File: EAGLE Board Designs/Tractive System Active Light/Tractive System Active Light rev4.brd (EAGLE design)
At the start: 67.5 x 26.9 mm, 10 parts, among them J1 CONNECTOR-4_μF_S_RA_

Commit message: updated led silkscreen
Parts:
- renumbered U$1 to D1, U$2 to D2, U$3 to D3, U$4 to D4
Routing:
- net N$9: track 16.0 -> 16.6 mm
- net N$7: track 19.6 -> 20.2 mm
- net N$2: track 20.5 -> 20.0 mm

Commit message: Update Tractive System Active Light rev4.brd
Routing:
- net N$2: track 20.0 -> 20.6 mm
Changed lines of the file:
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@@
 <contactref element="D4" pad="B+"/>
 <via x="-19.05" y="16.51" extent="1-16" drill="0.381"/>
-<wire x1="-13.3625" y1="18.685" x2="-13.39710625" y2="18.685" width="0.4064" layer="16"/>
-<wire x1="-13.39710625" y1="18.685" x2="-14.07770625" y2="19.3656" width="0.4064" layer="16"/>
-<wire x1="-14.07770625" y1="19.3656" x2="-16.1944" y2="19.3656" width="0.4064" layer="16"/>
-<wire x1="-16.1944" y1="19.3656" x2="-19.05" y2="16.51" width="0.4064" layer="16"/>
 <wire x1="-19.05" y1="16.51" x2="-20.6175" y2="16.51" width="0.4064" layer="1"/>
 <wire x1="-20.6175" y1="16.51" x2="-28.6025" y2="8.525" width="0.4064" layer="1"/>
+<wire x1="-13.3625" y1="18.685" x2="-13.3625" y2="18.9505" width="0.4064" layer="16"/>
+<wire x1="-13.3625" y1="18.9505" x2="-14.351" y2="19.939" width="0.4064" layer="16"/>
+<wire x1="-14.351" y1="19.939" x2="-15.621" y2="19.939" width="0.4064" layer="16"/>
+<wire x1="-15.621" y1="19.939" x2="-19.05" y2="16.51" width="0.4064" layer="16"/>
 </signal>
 </signals>

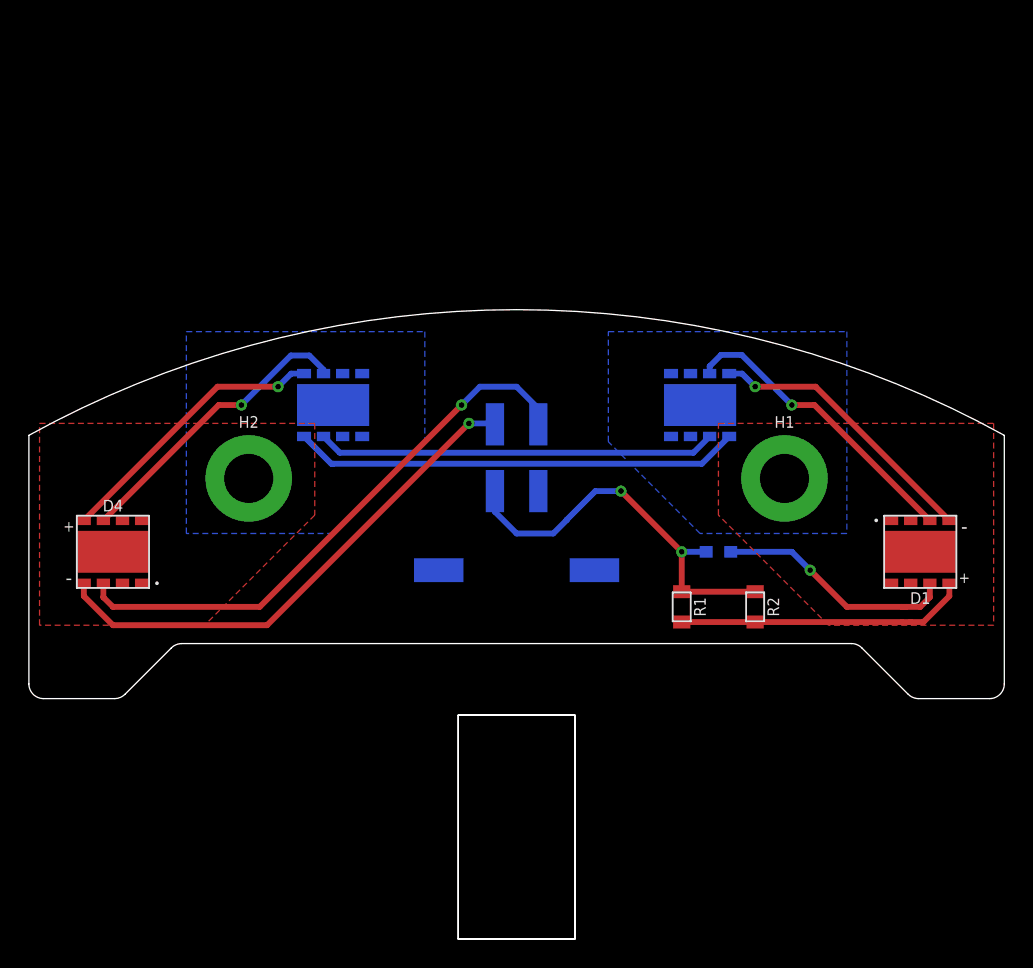
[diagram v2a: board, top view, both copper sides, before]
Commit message: moved connector to face upwards
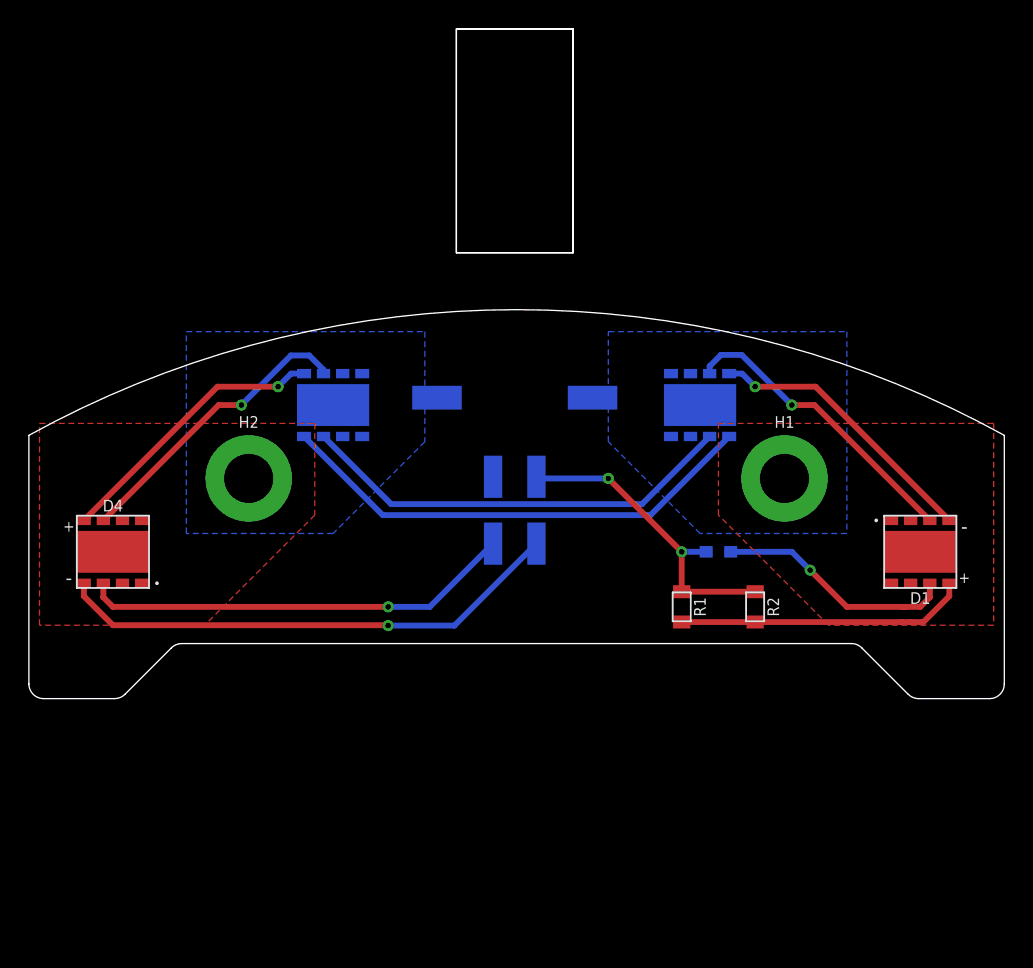
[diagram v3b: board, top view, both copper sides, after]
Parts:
- moved J1 11.9 mm to (-0.13, 17.0), turned to 180 degrees
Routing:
- net GND_GREEN: track 39.4 -> 30.0 mm
- net +12V: track 27.5 -> 21.7 mm
- net N$4: track 27.7 -> 30.6 mm
- net N$3: track 31.0 -> 33.9 mm
- net GND_RED: track 36.0 -> 35.4 mm
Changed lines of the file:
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@@
 <attribute name="VOLTAGE_MAX" value="150V" x="13.97" y="6.35" size="1.778" layer="28" rot="MR180" display="off"/>
 </element>
-<element name="J1" library="HyTechDevices" package="MOLEX_MICROFIT_SMD_RIGHTANGLE_04_DUAL" value="CONNECTOR-4_μF_S_RA_" x="0" y="5.08" smashed="yes" rot="MR0">
-<attribute name="DKPN" value="WM1832CT-ND" x="0" y="5.08" size="1.778" layer="28" rot="MR0" display="off"/>
-<attribute name="MANUFACTURER" value="Molex" x="0" y="5.08" size="1.778" layer="28" rot="MR0" display="off"/>
-<attribute name="MOPN" value="538-0430450411" x="0" y="5.08" size="1.778" layer="28" rot="MR0" display="off"/>
-<attribute name="MPN" value="0430450411" x="0" y="5.08" size="1.778" layer="28" rot="MR0" display="off"/>
-<attribute name="NAME" x="0" y="19.431" size="0.8128" layer="26" rot="MR180" align="bottom-center"/>
+<element name="J1" library="HyTechDevices" package="MOLEX_MICROFIT_SMD_RIGHTANGLE_04_DUAL" value="CONNECTOR-4_μF_S_RA_" x="-0.127" y="17.018" smashed="yes" rot="MR180">
+<attribute name="DKPN" value="WM1832CT-ND" x="-0.127" y="17.018" size="1.778" layer="28" rot="MR180" display="off"/>
+<attribute name="MANUFACTURER" value="Molex" x="-0.127" y="17.018" size="1.778" layer="28" rot="MR180" display="off"/>
+<attribute name="MOPN" value="538-0430450411" x="-0.127" y="17.018" size="1.778" layer="28" rot="MR180" display="off"/>
+<attribute name="MPN" value="0430450411" x="-0.127" y="17.018" size="1.778" layer="28" rot="MR180" display="off"/>
+<attribute name="NAME" x="-0.127" y="2.667" size="0.8128" layer="26" rot="MR0" align="bottom-center"/>
 </element>
 <element name="H1" library="HyTechDevices" package="MOUNTING_M3" value="MOUNTING_HEATSINK_M3" x="18.542" y="11.43" smashed="yes">
@@
 <signal name="N$3">
 <contactref element="D2" pad="A-"/>
-<wire x1="-12.7" y1="12.446" x2="12.8235" y2="12.446" width="0.4064" layer="16"/>
-<wire x1="12.8235" y1="12.446" x2="14.7125" y2="14.335" width="0.4064" layer="16"/>
+<wire x1="-14.7125" y1="14.335" x2="-9.2675" y2="8.89" width="0.4064" layer="16"/>
+<wire x1="9.2675" y1="8.89" x2="-9.2675" y2="8.89" width="0.4064" layer="16"/>
+<wire x1="9.2675" y1="8.89" x2="14.7125" y2="14.335" width="0.4064" layer="16"/>
 <contactref element="D3" pad="A+"/>
-<wire x1="-12.7" y1="12.446" x2="-12.8235" y2="12.446" width="0.4064" layer="16"/>
-<wire x1="-12.8235" y1="12.446" x2="-14.7125" y2="14.335" width="0.4064" layer="16"/>
 </signal>
 <signal name="N$4">
-<wire x1="12.2355" y1="13.208" x2="-12.2355" y2="13.208" width="0.4064" layer="16"/>
+<wire x1="8.6795" y1="9.652" x2="-8.6795" y2="9.652" width="0.4064" layer="16"/>
 <contactref element="D2" pad="B-"/>
-<wire x1="12.2355" y1="13.208" x2="13.3625" y2="14.335" width="0.4064" layer="16"/>
+<wire x1="8.6795" y1="9.652" x2="13.3625" y2="14.335" width="0.4064" layer="16"/>
 <contactref element="D3" pad="B+"/>
-<wire x1="-12.2355" y1="13.208" x2="-13.3625" y2="14.335" width="0.4064" layer="16"/>
+<wire x1="-8.6795" y1="9.652" x2="-13.3625" y2="14.335" width="0.4064" layer="16"/>
 </signal>
 <signal name="N$5">
@@
 </signal>
 <signal name="GND_RED">
-<wire x1="-27.94" y1="1.27" x2="-29.9525" y2="3.2825" width="0.4064" layer="1"/>
+<wire x1="-29.9525" y1="3.2825" x2="-27.94" y2="1.27" width="0.4064" layer="1"/>
 <contactref element="J1" pad="3"/>
-<wire x1="-27.94" y1="1.27" x2="-17.272" y2="1.27" width="0.4064" layer="1"/>
-<via x="-3.302" y="15.24" extent="1-16" drill="0.381"/>
-<wire x1="-17.272" y1="1.27" x2="-3.302" y2="15.24" width="0.4064" layer="1"/>
-<wire x1="-3.302" y1="15.24" x2="-1.5635" y2="15.24" width="0.4064" layer="16"/>
-<wire x1="-1.5635" y1="15.24" x2="-1.5" y2="15.1765" width="0.4064" layer="16"/>
 <contactref element="D4" pad="A-"/>
 <wire x1="-29.9525" y1="3.2825" x2="-29.9525" y2="4.175" width="0.4064" layer="1"/>
+<wire x1="-8.9154" y1="1.27" x2="-8.89" y2="1.2446" width="0.4064" layer="1"/>
+<via x="-8.89" y="1.2446" extent="1-16" drill="0.381"/>
+<wire x1="-8.89" y1="1.2446" x2="-4.3039" y2="1.2446" width="0.4064" layer="16"/>
+<wire x1="-4.3039" y1="1.2446" x2="1.373" y2="6.9215" width="0.4064" layer="16"/>
+<wire x1="-27.94" y1="1.27" x2="-8.9154" y2="1.27" width="0.4064" layer="1"/>
 </signal>
 <signal name="GND_GREEN">
-<wire x1="-27.94" y1="2.54" x2="-28.6025" y2="3.2025" width="0.4064" layer="1"/>
+<wire x1="-28.6025" y1="3.2025" x2="-27.94" y2="2.54" width="0.4064" layer="1"/>
 <contactref element="J1" pad="4"/>
-<wire x1="-27.94" y1="2.54" x2="-17.78" y2="2.54" width="0.4064" layer="1"/>
-<wire x1="-17.78" y1="2.54" x2="-3.81" y2="16.51" width="0.4064" layer="1"/>
-<via x="-3.81" y="16.51" extent="1-16" drill="0.381"/>
-<wire x1="-3.81" y1="16.51" x2="-2.54" y2="17.78" width="0.4064" layer="16"/>
-<wire x1="-2.54" y1="17.78" x2="0" y2="17.78" width="0.4064" layer="16"/>
-<wire x1="0" y1="17.78" x2="1.5" y2="16.28" width="0.4064" layer="16"/>
-<wire x1="1.5" y1="16.28" x2="1.5" y2="15.1765" width="0.4064" layer="16"/>
 <contactref element="D4" pad="B-"/>
 <wire x1="-28.6025" y1="3.2025" x2="-28.6025" y2="4.175" width="0.4064" layer="1"/>
+<via x="-8.89" y="2.54" extent="1-16" drill="0.381"/>
+<wire x1="-8.89" y1="2.54" x2="-6.0085" y2="2.54" width="0.4064" layer="16"/>
+<wire x1="-6.0085" y1="2.54" x2="-1.627" y2="6.9215" width="0.4064" layer="16"/>
+<wire x1="-27.94" y1="2.54" x2="-8.89" y2="2.54" width="0.4064" layer="1"/>
 </signal>
 <signal name="+12V">
@@
 <wire x1="11.43" y1="3.59" x2="16.51" y2="3.59" width="0.4064" layer="1"/>
 <contactref element="J1" pad="1"/>
-<wire x1="7.2263" y1="10.5537" x2="11.43" y2="6.35" width="0.4064" layer="1"/>
 <wire x1="11.43" y1="6.35" x2="11.43" y2="3.59" width="0.4064" layer="1"/>
 <via x="11.43" y="6.35" extent="1-16" drill="0.381"/>
 <wire x1="11.43" y1="6.35" x2="13.12" y2="6.35" width="0.4064" layer="16"/>
-<via x="7.2263" y="10.5537" extent="1-16" drill="0.381"/>
-<wire x1="3.4685" y1="8.56776875" x2="3.4685" y2="8.5485" width="0.4064" layer="16"/>
-<wire x1="3.4685" y1="8.5485" x2="2.54" y2="7.62" width="0.4064" layer="16"/>
-<wire x1="7.2263" y1="10.5537" x2="5.45443125" y2="10.5537" width="0.4064" layer="16"/>
-<wire x1="5.45443125" y1="10.5537" x2="3.4685" y2="8.56776875" width="0.4064" layer="16"/>
-<wire x1="2.54" y1="7.62" x2="0" y2="7.62" width="0.4064" layer="16"/>
-<wire x1="0" y1="7.62" x2="-1.5" y2="9.12" width="0.4064" layer="16"/>
-<wire x1="-1.5" y1="9.12" x2="-1.5" y2="10.5537" width="0.4064" layer="16"/>
+<via x="6.35" y="11.43" extent="1-16" drill="0.381"/>
+<wire x1="6.35" y1="11.43" x2="1.4873" y2="11.43" width="0.4064" layer="16"/>
+<wire x1="1.4873" y1="11.43" x2="1.373" y2="11.5443" width="0.4064" layer="16"/>
+<wire x1="11.43" y1="6.35" x2="6.35" y2="11.43" width="0.4064" layer="1"/>
 </signal>
 <signal name="N$8">

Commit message: Update Tractive System Active Light rev4.brd
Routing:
- net GND_RED: track 35.4 -> 37.1 mm
- net GND_GREEN: track 30.0 -> 31.5 mm
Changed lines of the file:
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@@
 <drawing>
 <settings>
-<setting alwaysvectorfont="no"/>
+<setting alwaysvectorfont="yes"/>
 <setting verticaltext="up"/>
 </settings>
@@
 <wire x1="-8.9154" y1="1.27" x2="-8.89" y2="1.2446" width="0.4064" layer="1"/>
 <via x="-8.89" y="1.2446" extent="1-16" drill="0.381"/>
-<wire x1="-8.89" y1="1.2446" x2="-4.3039" y2="1.2446" width="0.4064" layer="16"/>
-<wire x1="-4.3039" y1="1.2446" x2="1.373" y2="6.9215" width="0.4064" layer="16"/>
+<wire x1="-8.89" y1="1.2446" x2="-1.5099" y2="1.2446" width="0.4064" layer="16"/>
+<wire x1="1.373" y1="4.1275" x2="1.373" y2="6.9215" width="0.4064" layer="16"/>
+<wire x1="1.373" y1="4.1275" x2="-1.5099" y2="1.2446" width="0.4064" layer="16"/>
 <wire x1="-27.94" y1="1.27" x2="-8.9154" y2="1.27" width="0.4064" layer="1"/>
 </signal>
@@
 <wire x1="-28.6025" y1="3.2025" x2="-28.6025" y2="4.175" width="0.4064" layer="1"/>
 <via x="-8.89" y="2.54" extent="1-16" drill="0.381"/>
-<wire x1="-8.89" y1="2.54" x2="-6.0085" y2="2.54" width="0.4064" layer="16"/>
-<wire x1="-6.0085" y1="2.54" x2="-1.627" y2="6.9215" width="0.4064" layer="16"/>
+<wire x1="-8.89" y1="2.54" x2="-3.4685" y2="2.54" width="0.4064" layer="16"/>
+<wire x1="-1.627" y1="4.3815" x2="-1.627" y2="6.9215" width="0.4064" layer="16"/>
+<wire x1="-1.627" y1="4.3815" x2="-3.4685" y2="2.54" width="0.4064" layer="16"/>
 <wire x1="-27.94" y1="2.54" x2="-8.89" y2="2.54" width="0.4064" layer="1"/>
 </signal>

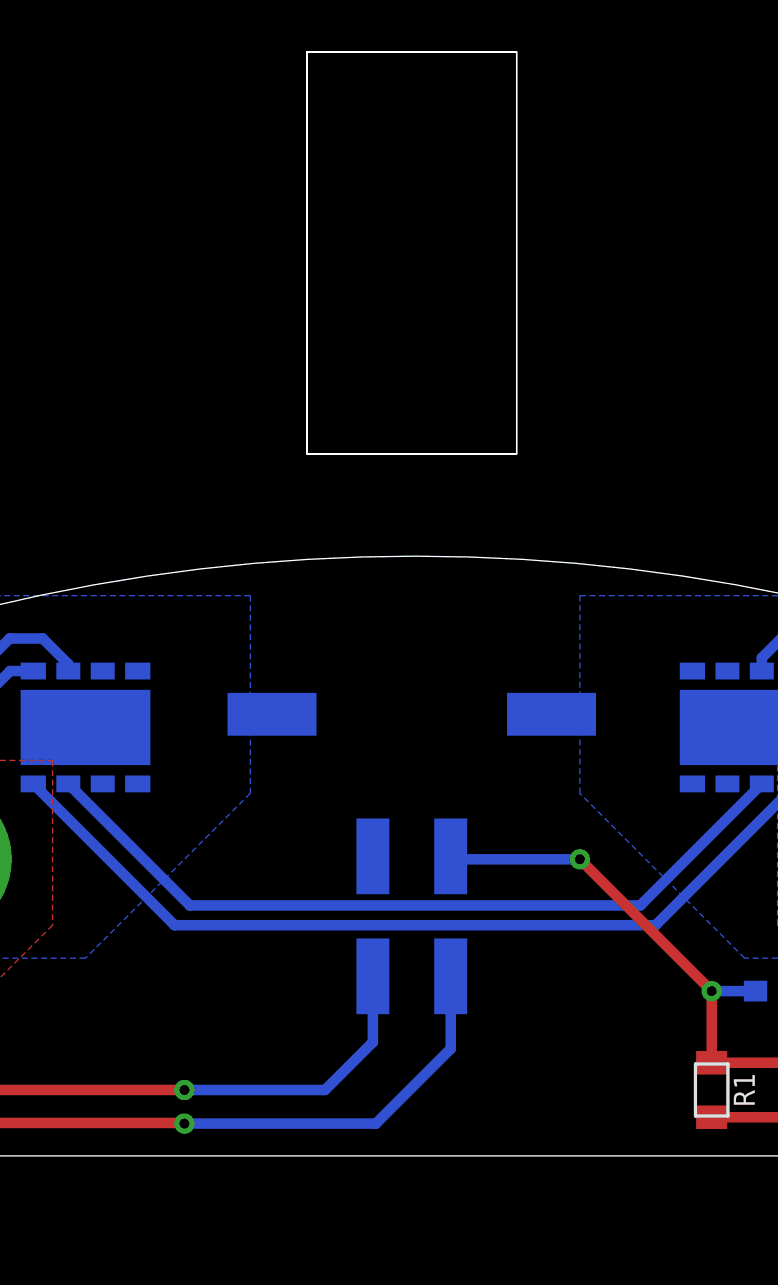
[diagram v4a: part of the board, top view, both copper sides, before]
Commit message: centered connector
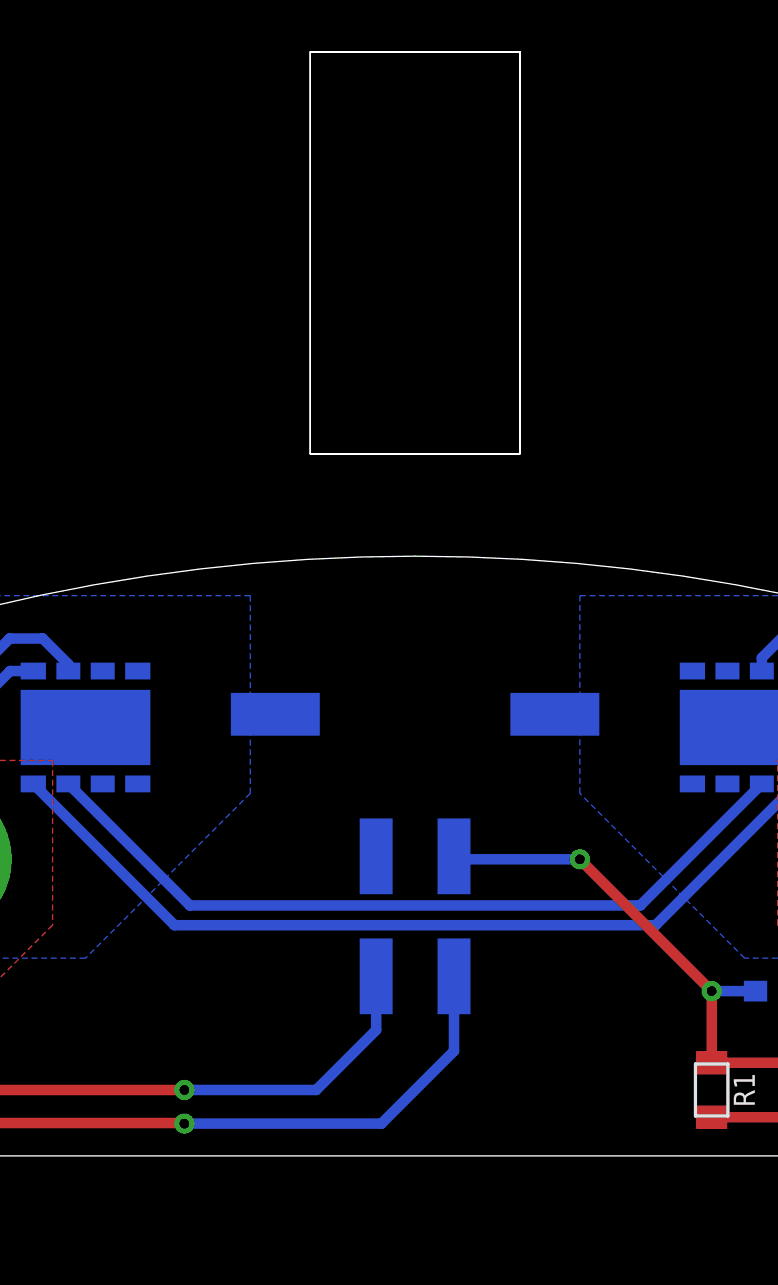
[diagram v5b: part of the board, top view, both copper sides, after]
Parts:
- moved J1 0.13 mm to (0.00, 17.0)
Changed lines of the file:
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@@
 <attribute name="VOLTAGE_MAX" value="150V" x="13.97" y="6.35" size="1.778" layer="28" rot="MR180" display="off"/>
 </element>
-<element name="J1" library="HyTechDevices" package="MOLEX_MICROFIT_SMD_RIGHTANGLE_04_DUAL" value="CONNECTOR-4_μF_S_RA_" x="-0.127" y="17.018" smashed="yes" rot="MR180">
-<attribute name="DKPN" value="WM1832CT-ND" x="-0.127" y="17.018" size="1.778" layer="28" rot="MR180" display="off"/>
-<attribute name="MANUFACTURER" value="Molex" x="-0.127" y="17.018" size="1.778" layer="28" rot="MR180" display="off"/>
-<attribute name="MOPN" value="538-0430450411" x="-0.127" y="17.018" size="1.778" layer="28" rot="MR180" display="off"/>
-<attribute name="MPN" value="0430450411" x="-0.127" y="17.018" size="1.778" layer="28" rot="MR180" display="off"/>
-<attribute name="NAME" x="-0.127" y="2.667" size="0.8128" layer="26" rot="MR0" align="bottom-center"/>
+<element name="J1" library="HyTechDevices" package="MOLEX_MICROFIT_SMD_RIGHTANGLE_04_DUAL" value="CONNECTOR-4_μF_S_RA_" x="0" y="17.018" smashed="yes" rot="MR180">
+<attribute name="DKPN" value="WM1832CT-ND" x="0" y="17.018" size="1.778" layer="28" rot="MR180" display="off"/>
+<attribute name="MANUFACTURER" value="Molex" x="0" y="17.018" size="1.778" layer="28" rot="MR180" display="off"/>
+<attribute name="MOPN" value="538-0430450411" x="0" y="17.018" size="1.778" layer="28" rot="MR180" display="off"/>
+<attribute name="MPN" value="0430450411" x="0" y="17.018" size="1.778" layer="28" rot="MR180" display="off"/>
+<attribute name="NAME" x="0" y="2.667" size="0.8128" layer="26" rot="MR0" align="bottom-center"/>
 </element>
 <element name="H1" library="HyTechDevices" package="MOUNTING_M3" value="MOUNTING_HEATSINK_M3" x="18.542" y="11.43" smashed="yes">
@@
 <wire x1="-8.9154" y1="1.27" x2="-8.89" y2="1.2446" width="0.4064" layer="1"/>
 <via x="-8.89" y="1.2446" extent="1-16" drill="0.381"/>
-<wire x1="-8.89" y1="1.2446" x2="-1.5099" y2="1.2446" width="0.4064" layer="16"/>
-<wire x1="1.373" y1="4.1275" x2="1.373" y2="6.9215" width="0.4064" layer="16"/>
-<wire x1="1.373" y1="4.1275" x2="-1.5099" y2="1.2446" width="0.4064" layer="16"/>
 <wire x1="-27.94" y1="1.27" x2="-8.9154" y2="1.27" width="0.4064" layer="1"/>
+<wire x1="-8.89" y1="1.2446" x2="-1.2954" y2="1.2446" width="0.4064" layer="16"/>
+<wire x1="1.5" y1="4.04" x2="1.5" y2="6.9215" width="0.4064" layer="16"/>
+<wire x1="-1.2954" y1="1.2446" x2="1.5" y2="4.04" width="0.4064" layer="16"/>
 </signal>
 <signal name="GND_GREEN">
@@
 <wire x1="-28.6025" y1="3.2025" x2="-28.6025" y2="4.175" width="0.4064" layer="1"/>
 <via x="-8.89" y="2.54" extent="1-16" drill="0.381"/>
-<wire x1="-8.89" y1="2.54" x2="-3.4685" y2="2.54" width="0.4064" layer="16"/>
-<wire x1="-1.627" y1="4.3815" x2="-1.627" y2="6.9215" width="0.4064" layer="16"/>
-<wire x1="-1.627" y1="4.3815" x2="-3.4685" y2="2.54" width="0.4064" layer="16"/>
 <wire x1="-27.94" y1="2.54" x2="-8.89" y2="2.54" width="0.4064" layer="1"/>
+<wire x1="-8.89" y1="2.54" x2="-3.81" y2="2.54" width="0.4064" layer="16"/>
+<wire x1="-1.5" y1="4.85" x2="-1.5" y2="6.9215" width="0.4064" layer="16"/>
+<wire x1="-3.81" y1="2.54" x2="-1.5" y2="4.85" width="0.4064" layer="16"/>
 </signal>
 <signal name="+12V">
@@
 <wire x1="11.43" y1="6.35" x2="13.12" y2="6.35" width="0.4064" layer="16"/>
 <via x="6.35" y="11.43" extent="1-16" drill="0.381"/>
-<wire x1="6.35" y1="11.43" x2="1.4873" y2="11.43" width="0.4064" layer="16"/>
-<wire x1="1.4873" y1="11.43" x2="1.373" y2="11.5443" width="0.4064" layer="16"/>
 <wire x1="11.43" y1="6.35" x2="6.35" y2="11.43" width="0.4064" layer="1"/>
+<wire x1="6.35" y1="11.43" x2="1.6143" y2="11.43" width="0.4064" layer="16"/>
+<wire x1="1.6143" y1="11.43" x2="1.5" y2="11.5443" width="0.4064" layer="16"/>
 </signal>
 <signal name="N$8">
